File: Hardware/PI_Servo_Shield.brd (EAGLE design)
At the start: 65 x 30 mm, 46 parts, among them J1 RASPBERRYPI-40-PIN-GPIO_PTH, U1 FT231XS, U2 PCA9306, U3 PCA9685

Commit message: Changes based on talk with Adam
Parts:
- added FD1, FD2: FIDUCIALUFIDUCIAL, SparkFun-Aesthetics:FIDUCIAL-MICRO
- added LOGO1: SFE_LOGO_NAME_FLAME.1_INCH, SparkFun-Aesthetics:SFE_LOGO_NAME_FLAME_.1
- added LOGO2: OSHW-LOGOM, SparkFun-Aesthetics:OSHW-LOGO-M
- J1: value RASPBERRYPI-40-PIN-GPIO_PTH -> RASPBERRYPI-40-PIN-GPIO_PTH_NO_SHROUD; device SparkFun-Connectors:2X20_SHROUDED -> SparkFun-Connectors:2X20
- moved J1 24.2 mm to (8.34, 25.3), turned to 0 degrees
- moved J10 1.90 mm to (29.2, 1.27)
- moved J6 1.90 mm to (16.5, 1.27)
- moved J11 1.27 mm to (35.6, 1.27)
- moved J5 1.27 mm to (14.0, 1.27)
- moved J9 1.27 mm to (26.7, 1.27)
- moved J15 1.27 mm to (48.3, 1.27)
- moved J8 0.64 mm to (24.1, 1.27)
- moved J4 0.63 mm to (11.4, 1.27)
- moved J12 0.63 mm to (38.1, 1.27)
- moved J14 0.63 mm to (43.2, 1.27)
- moved J16 0.63 mm to (50.8, 1.27)
- moved J18 0.63 mm to (55.9, 1.27)
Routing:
- net CH2: track 19.5 -> 23.0 mm
- net CH3: track 16.1 -> 19.6 mm
- net CH8: track 9.02 -> 5.71 mm
- net CH1: track 23.0 -> 26.2 mm
- net CH0: track 26.4 -> 29.6 mm
- net 3.3VA: track 36.9 -> 39.3 mm
- net CH12: track 12.2 -> 14.4 mm
- net CH9: track 7.16 -> 5.12 mm
- net CH13: track 15.6 -> 17.2 mm
- net CH5: track 9.21 -> 10.7 mm
- net CH6: track 6.73 -> 8.22 mm
- net CH4: track 12.7 -> 13.6 mm
- net CH14: track 19.0 -> 19.8 mm
- net VIN: track 90.8 -> 90.2 mm
- net CH7: track 5.01 -> 5.56 mm
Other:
- board text added: "0"
- board text added: "1"
- board text added: "10"
- board text added: "11"
- board text added: "12"
- board text added: "13"
- board text added: "14"
- board text added: "15"
- board text added: "2"
- board text added: "3"
- board text added: "4"
- board text added: "5"
- board text added: "6"
- board text added: "7"
- board text added: "8"
- board text added: "9"
- board text added: "Pi Servo Shield"

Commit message: Changes from review feedback
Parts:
- added FD3, FD4: FIDUCIALUFIDUCIAL, SparkFun-Aesthetics:FIDUCIAL-MICRO
- moved FD2 88.8 mm to (63.5, 24.1)
- moved FD1 33.0 mm to (2.54, 7.62)
- moved C4 1.27 mm to (39.0, 20.6)
- moved C3 1.27 mm to (25.4, 14.0)
- moved D2 1.27 mm to (8.89, 14.0)
- moved R4 1.27 mm to (56.0, 16.5)
- moved R5 1.27 mm to (54.5, 16.5)
- moved R7 1.27 mm to (12.7, 14.0)
- moved U2 1.27 mm to (51.4, 16.5)
- moved C1 1.27 mm to (9.53, 17.8)
- moved C2 1.27 mm to (11.3, 17.8)
- moved C7 1.27 mm to (53.0, 13.6)
- moved C8 1.27 mm to (47.6, 14.2)
- moved D1 1.27 mm to (8.89, 12.4)
- moved J2 1.27 mm to (1.98, 15.0)
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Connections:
- new net SHIELD: J2.SHIELD1, J2.SHIELD2, J2.SHIELD3
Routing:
- net VIN: track 90.2 -> 82.5 mm
- net 5VB: track 63.6 -> 61.1 mm
- net 3.3VA: track 39.3 -> 37.3 mm
- net LV_SDA: track 54.8 -> 53.5 mm
- net LV_SCL: track 54.4 -> 53.1 mm
- net RXD: track 20.5 -> 19.2 mm
- net CH5: track 10.7 -> 12.0 mm
- net CH2: track 23.0 -> 24.3 mm
- net CH15: track 22.6 -> 23.8 mm
- net CH1: track 26.2 -> 27.5 mm
- net CH0: track 29.6 -> 30.9 mm
- net CH11: track 9.30 -> 10.6 mm
- net TXD: track 19.3 -> 18.0 mm
- net CH9: track 5.12 -> 6.39 mm
- net CH8: track 5.71 -> 6.98 mm
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- added copper zone on layer 1, net SHIELD
- added copper zone on layer 16, net SHIELD
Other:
- board text added: "GND"
- board text added: "POW"
- board text added: "SIG"
- board text added: "VIN ISO"

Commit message: Addressed errors from double check
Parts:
- D1: value Yellow -> GREEN
- D2: value Red -> Yellow
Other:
- board text added: "RX"
- board text added: "TX"
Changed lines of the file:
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@@
 <layer number="2" name="Route2" color="1" fill="3" visible="no" active="yes"/>
 <layer number="15" name="Route15" color="4" fill="6" visible="no" active="yes"/>
-<layer number="16" name="Bottom" color="1" fill="1" visible="no" active="yes"/>
+<layer number="16" name="Bottom" color="1" fill="1" visible="yes" active="yes"/>
 <layer number="17" name="Pads" color="2" fill="1" visible="yes" active="yes"/>
 <layer number="18" name="Vias" color="2" fill="1" visible="yes" active="yes"/>
@@
 <layer number="20" name="Dimension" color="15" fill="1" visible="yes" active="yes"/>
 <layer number="21" name="tPlace" color="16" fill="1" visible="yes" active="yes"/>
-<layer number="22" name="bPlace" color="14" fill="1" visible="no" active="yes"/>
+<layer number="22" name="bPlace" color="14" fill="1" visible="yes" active="yes"/>
 <layer number="23" name="tOrigins" color="15" fill="1" visible="yes" active="yes"/>
-<layer number="24" name="bOrigins" color="15" fill="1" visible="no" active="yes"/>
+<layer number="24" name="bOrigins" color="15" fill="1" visible="yes" active="yes"/>
 <layer number="25" name="tNames" color="7" fill="1" visible="no" active="yes"/>
 <layer number="26" name="bNames" color="7" fill="1" visible="no" active="yes"/>
@@
 <layer number="43" name="vRestrict" color="2" fill="10" visible="no" active="yes"/>
 <layer number="44" name="Drills" color="7" fill="1" visible="no" active="yes"/>
-<layer number="45" name="Holes" color="7" fill="1" visible="no" active="yes"/>
+<layer number="45" name="Holes" color="7" fill="1" visible="yes" active="yes"/>
 <layer number="46" name="Milling" color="3" fill="1" visible="no" active="yes"/>
 <layer number="47" name="Measures" color="7" fill="1" visible="no" active="yes"/>
 <layer number="48" name="Document" color="7" fill="1" visible="no" active="yes"/>
 <layer number="49" name="Reference" color="7" fill="1" visible="no" active="yes"/>
-<layer number="51" name="tDocu" color="6" fill="1" visible="no" active="yes"/>
+<layer number="51" name="tDocu" color="6" fill="1" visible="yes" active="yes"/>
 <layer number="52" name="bDocu" color="7" fill="1" visible="no" active="yes"/>
 <layer number="3" name="Route3" color="4" fill="3" visible="no" active="no"/>
@@
 <text x="31.115" y="0.762" size="1.016" layer="21" font="vector" ratio="15">GND</text>
 <text x="31.242" y="5.842" size="1.016" layer="21" font="vector" ratio="15">SIG</text>
+<text x="8.89" y="10.922" size="0.8128" layer="21" font="vector" ratio="15">TX</text>
+<text x="9.144" y="14.605" size="0.8128" layer="21" font="vector" ratio="15">RX</text>
 </plain>
 <attributes>
@@
 <attribute name="PROD_ID" value="CAP-08604" x="25.4" y="13.97" size="1.778" layer="27" display="off"/>
 </element>
-<element name="D1" library="SparkFun-LED" package="LED-0603" value="Yellow" x="8.89" y="12.446">
-<attribute name="PROD_ID" value="DIO-11230" x="8.89" y="12.446" size="1.778" layer="27" display="off"/>
-</element>
-<element name="D2" library="SparkFun-LED" package="LED-0603" value="Red" x="8.89" y="13.97">
-<attribute name="PROD_ID" value="DIO-11154" x="8.89" y="13.97" size="1.778" layer="27" display="off"/>
+<element name="D1" library="SparkFun-LED" package="LED-0603" value="GREEN" x="8.89" y="12.446">
+<attribute name="PROD_ID" value="DIO-00821" x="8.89" y="12.446" size="1.778" layer="27" display="off"/>
+</element>
+<element name="D2" library="SparkFun-LED" package="LED-0603" value="Yellow" x="8.89" y="13.97">
+<attribute name="PROD_ID" value="DIO-11230" x="8.89" y="13.97" size="1.778" layer="27" display="off"/>
 </element>
 <element name="FRAME1" library="SparkFun-Aesthetics" package="CREATIVE_COMMONS" value="FRAME-LETTER" x="24.13" y="-20.32"/>
@@
 <contactref element="C7" pad="2"/>
 <contactref element="C8" pad="2"/>
+<via x="19.05" y="14.097" extent="1-16" drill="0.381"/>
+<via x="24.511" y="15.494" extent="1-16" drill="0.381"/>
+<via x="41.021" y="16.129" extent="1-16" drill="0.381"/>
 </signal>
 <signal name="LV_SCL">

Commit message: Change version number
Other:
- board text added: "v10"
- board text removed: "v00"
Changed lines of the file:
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@@
 <wire x1="65" y1="27" x2="65" y2="3" width="0.2032" layer="20"/>
 <wire x1="65" y1="3" x2="62" y2="0" width="0.2032" layer="20" curve="-90"/>
-<text x="64.262" y="12.319" size="1.778" layer="16" font="vector" ratio="15" rot="MR270">v00</text>
+<text x="64.262" y="12.319" size="1.778" layer="16" font="vector" ratio="15" rot="MR270">v10</text>
 <text x="54.61" y="-20.32" size="1.778" layer="51" font="vector" ratio="15">M. Hord</text>
 <dimension x1="0" y1="30" x2="65" y2="30" x3="32.5" y3="39" textsize="1.778" textratio="15" layer="47" dtype="horizontal"/>

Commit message: Change to v10
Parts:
- moved H3 0.50 mm to (61.5, 26.5)
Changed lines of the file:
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@@
 <element name="H1" library="SparkFun-Hardware" package="STAND-OFF" value="STAND-OFF" x="61.5" y="3.5"/>
 <element name="H2" library="SparkFun-Hardware" package="STAND-OFF" value="STAND-OFF" x="3.5" y="26.5"/>
-<element name="H3" library="SparkFun-Hardware" package="STAND-OFF" value="STAND-OFF" x="61" y="26.5"/>
+<element name="H3" library="SparkFun-Hardware" package="STAND-OFF" value="STAND-OFF" x="61.5" y="26.5"/>
 <element name="H4" library="SparkFun-Hardware" package="STAND-OFF" value="STAND-OFF" x="3.5" y="3.5"/>
 <element name="C4" library="SparkFun-Capacitors" package="0603" value="0.1uF" x="38.989" y="20.574">

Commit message: v20 hardwaer 99% done - still needs buzzard migration
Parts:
- removed C1, C2: 47pF, SparkFun-Capacitors:0603
- removed D1: GREEN, SparkFun-LED:LED-0603
- removed D2: Yellow, SparkFun-LED:LED-0603
- removed J2: (no value), SparkFun-Connectors:USB-B-MICRO-SMD
- removed R6, R7: 1k, SparkFun-Resistors:0603
- removed R8, R9: 27, SparkFun-Resistors:0603
- removed U1: FT231XS, SparkFun-IC-Comms:SSOP20_L
- added C10: 0.1uF, SparkFun-Capacitors:0603
- added C17: 10nF, SparkFun-Capacitors:0603
- added D3: Yellow, SparkFun-LED:LED-1206-HIDDENSILK
- added D4: GREEN, SparkFun-LED:LED-1206
- added F2: 6V/2A, SparkFun-Fuses:1210
- added J19: (no value), SparkFun-Connectors:JST04_1MM_RA
- added J20: USB C, USB-C:USB-C-16P
- added J21: (no value), SparkFun-Connectors:1X04
- added JP2: (no value), SparkFun-Jumpers:SMT-JUMPER_2_NO_SILK
- added JP3: I2C, SparkFun-Jumpers:SMT-JUMPER_3_2-NC_TRACE_SILK
- added R10, R11: 5.1k, SparkFun-Resistors:0603
- added R12, R16: 4.7k, SparkFun-Resistors:0603
- added U$1: QWIIC_LOGO_3MM, SparkFun-Aesthetics:QWIIC_3MM
- added U5: CH340C, SparkFun-IC-Comms:SO016
- JP1: value JUMPER-SMT_2_NC_PASTE_NO-SILK -> VIN ISO
- LOGO2: value OSHW-LOGOM -> OSHW-LOGOS; device SparkFun-Aesthetics:OSHW-LOGO-M -> SparkFun-Aesthetics:OSHW-LOGO-S
- moved C3 14.8 mm to (12.8, 21.6), turned to 180 degrees
- moved LOGO2 14.2 mm to (50.8, 34.3)
- moved LOGO1 9.33 mm to (42.8, 18.0)
- moved J3 8.89 mm to (17.8, 1.27)
- moved J4 8.89 mm to (20.3, 1.27)
- moved J5 8.89 mm to (22.9, 1.27)
- moved J6 8.89 mm to (25.4, 1.27)
- moved C6 7.54 mm to (13.3, 4.65)
- moved FD1 6.86 mm to (2.54, 0.76)
- moved FD3 6.86 mm to (2.54, 0.76)
- moved J10 6.35 mm to (35.6, 1.27)
- moved J7 6.35 mm to (27.9, 1.27)
- moved J8 6.35 mm to (30.5, 1.27)
- moved J9 6.35 mm to (33.0, 1.27)
- moved R3 5.83 mm to (43.7, 11.4)
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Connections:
- removed net N$10: C2.1, J2.D+, R9.1
- removed net N$11: C1.1, J2.D-, R8.1
- removed net N$6: D1.C, R6.2
- removed net N$7: R7.1, U1.17
- removed net N$8: R6.1, U1.10
- removed net N$9: R9.2, U1.11
- removed net RXD: J1.8, U1.4
- removed net SHIELD: J2.SHIELD1, J2.SHIELD2, J2.SHIELD3
- removed net TXD: J1.10, U1.20
- new net CC1: J20.A5, R11.2
- new net CC2: J20.B5, R10.2
- new net D+: J20.A6, J20.B6, U5.5
- new net D-: J20.A7, J20.B7, U5.6
- new net N$12: D4.A, R16.1
- new net N$13: D3.A, R12.1
- new net N$14: C17.1, U5.4
- new net RXI: D4.C, J1.8, J21.1, U5.3
- new net SHLD: J20.SHLD1, J20.SHLD2, J20.SHLD3, J20.SHLD4, J20.SHLD5, J20.SHLD6, J20.SHLD7, J20.SHLD8
- new net TXO: D3.C, J1.10, J21.2, U5.2
- new net VBUS: C10.1, F2.1, J20.VBUS1, J20.VBUS2, JP2.1
- net 3.3VA: now also R12.2, R16.2, U5.16; no longer D1.A, D2.A, U1.14, U1.3
- net 3.3VB: now also J19.2, JP3.2; no longer R4.2, R5.2
- net 5VB: now also J21.4; no longer U1.15
- net GND: now also C10.2, C17.2, J19.1, J20.GND, J20.GND2, J21.3, R10.1, R11.1, U5.1; no longer C1.2, C2.2, J2.GND, U1.16, U1.6
- net LV_SCL: now also J19.4
- net LV_SDA: now also J19.3
- net N$2: now also JP3.3, R4.2; no longer R8.2, U1.12
- net N$5: now also JP3.1, R5.2; no longer D2.C, R7.2
- net VIN: now also F2.2, JP2.2; no longer J2.VBUS
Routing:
- net TXO: track 0.00 -> 33.8 mm, vias 0 -> 1
- net RXI: track 0.00 -> 28.4 mm, vias 0 -> 1
- net VBUS: track 0.00 -> 21.4 mm, vias 0 -> 2
- net N$8: track 19.3 -> 0.00 mm
- net RXD: track 19.2 -> 0.00 mm
- net TXD: track 18.0 -> 0.00 mm, vias 1 -> 0
- net LV_SCL: track 53.1 -> 69.7 mm, vias 2 -> 0
- net N$11: track 16.4 -> 0.00 mm
- net 3.3VA: track 37.3 -> 21.2 mm, vias 1 -> 0
- net N$10: track 11.9 -> 0.00 mm
- net CH0: track 30.9 -> 20.7 mm
- net N$14: track 0.00 -> 10.0 mm
- net CH1: track 27.5 -> 17.9 mm
- net CH2: track 24.3 -> 14.9 mm
- net CH3: track 20.8 -> 11.9 mm
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- added copper zone on layer 1, net SHLD
- added copper zone on layer 16, net SHLD
- removed copper zone on layer 1, net SHIELD
- removed copper zone on layer 16, net SHIELD
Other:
- board text added: "5V"
- board text added: "JP2"
- board text added: "Pete Lewis"
- board text added: "Revised by:"
- board text added: "v20"
- board text removed: "POW"
- board text removed: "v10"

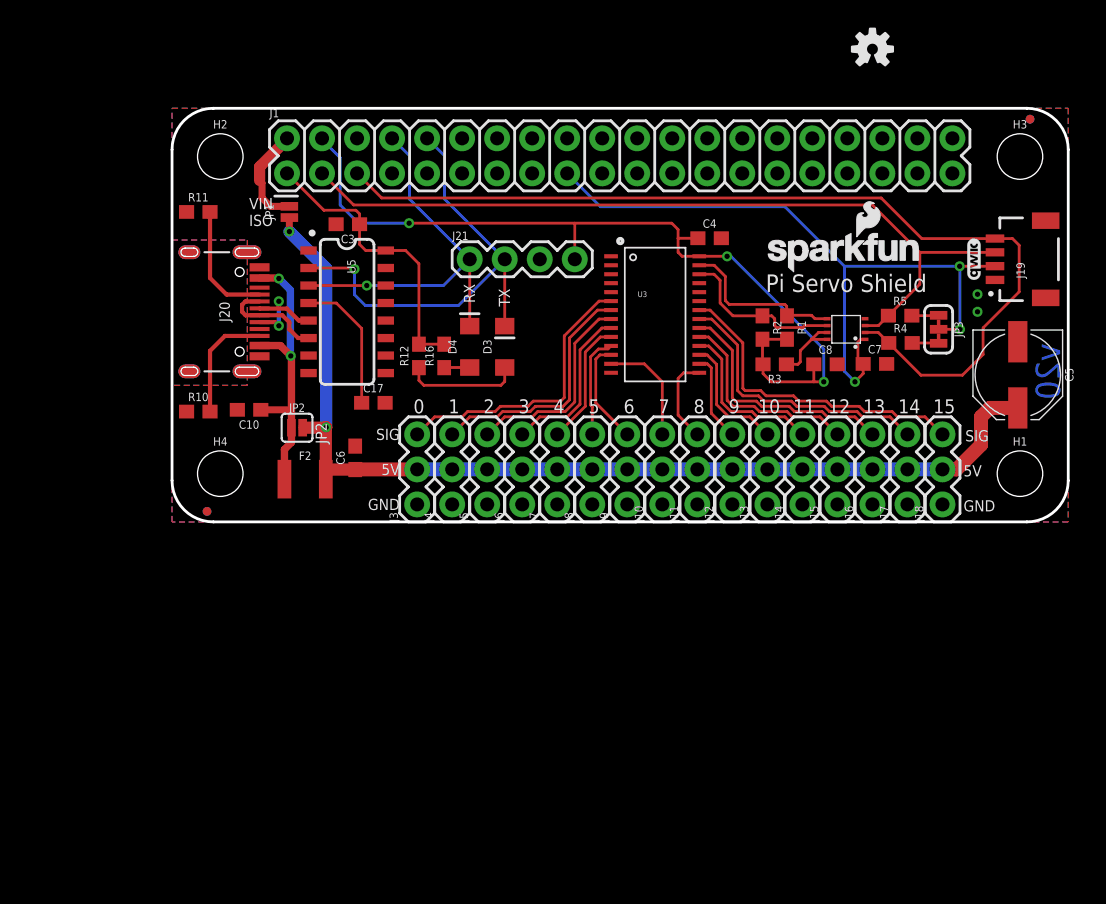
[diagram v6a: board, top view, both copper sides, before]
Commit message: Buzzard migration complete
Also nudged some stuff to avoid silk on vias and to make room for a few labels.
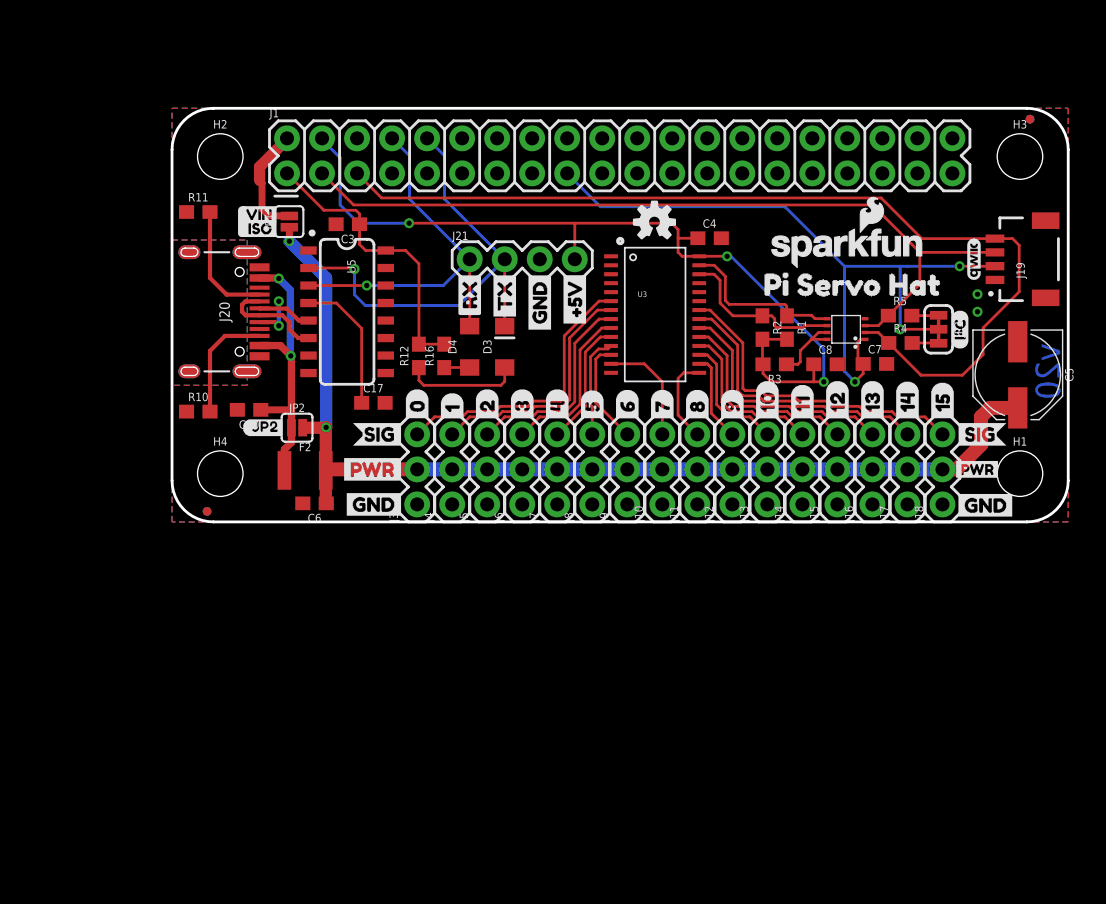
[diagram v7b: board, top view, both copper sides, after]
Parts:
- added U$10: (no value), buzzard_labels:735
- added U$11: (no value), buzzard_labels:836
- added U$12: (no value), buzzard_labels:937
- added U$13: (no value), buzzard_labels:1038
- added U$14: (no value), buzzard_labels:1139
- added U$15: (no value), buzzard_labels:1240
- added U$16: (no value), buzzard_labels:1341
- added U$17: (no value), buzzard_labels:1442
- added U$18: (no value), buzzard_labels:1543
- added U$19, U$23, U$28: (no value), buzzard_labels:GND25
- added U$2: (no value), Qwiic RFID - IDXXLA:I_SUPER2_C-()-03
- added U$20: (no value), buzzard_labels:PWR1
- added U$21: (no value), buzzard_labels:SIG2
- added U$22: (no value), buzzard_labels:SIG3
- added U$24: (no value), buzzard_labels2:PWR0
- added U$26: (no value), buzzard_labels (1):PI_SERVO_HAT0
- added U$27: (no value), buzzard_labels:#5V26
- added U$29: (no value), buzzard_labels:RX23
- added U$3: (no value), buzzard_labels:028
- added U$30: (no value), buzzard_labels:TX24
- added U$31: (no value), buzzard_labels (3):VIN0
- added U$32: (no value), buzzard_labels (3):ISO1
- added U$33: (no value), buzzard_labels (4):JP20
- added U$4: (no value), buzzard_labels:129
- added U$5: (no value), buzzard_labels:230
- added U$6: (no value), buzzard_labels:331
- added U$7: (no value), buzzard_labels:432
- added U$8: (no value), buzzard_labels:533
- added U$9: (no value), buzzard_labels:634
- JP1: device SparkFun-Jumpers:SMT-JUMPER_2_NC_PASTE_NO-SILK -> SparkFun-Jumpers:SMT-JUMPER_2_NC_PASTE_SILK
- moved LOGO2 20.2 mm to (35.0, 21.7)
- moved C6 4.43 mm to (10.3, 1.35), turned to 180 degrees
- moved JP1 0.70 mm to (8.51, 21.8)
- moved F2 0.63 mm to (9.65, 3.73)
- moved LOGO1 0.41 mm to (43.1, 18.4)
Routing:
- net VIN: track 75.1 -> 76.5 mm
- net 3.3VB: track 52.6 -> 53.8 mm
- net 5VA: track 7.46 -> 8.21 mm
- net VBUS: track 21.4 -> 20.7 mm
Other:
- board text removed: "0"
- board text removed: "1"
- board text removed: "10"
- board text removed: "11"
- board text removed: "12"
- board text removed: "13"
- board text removed: "14"
- board text removed: "15"
- board text removed: "2"
- board text removed: "3"
- board text removed: "4"
- board text removed: "5"
- board text removed: "5V"
- board text removed: "6"
- board text removed: "7"
- board text removed: "8"
- board text removed: "9"
- board text removed: "GND"
- board text removed: "JP2"
- board text removed: "Pi Servo Shield"
- board text removed: "RX"
- board text removed: "SIG"
- board text removed: "TX"
- board text removed: "VIN ISO"
